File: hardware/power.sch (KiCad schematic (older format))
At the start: 1 part, among them U5 MCP1755

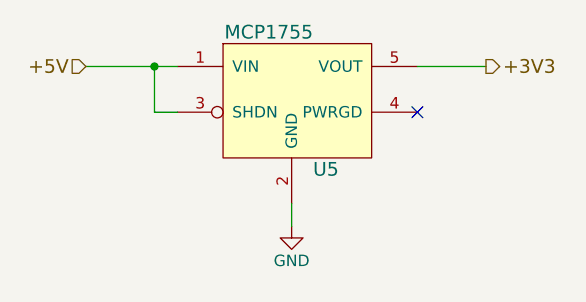
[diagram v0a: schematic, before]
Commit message: devboard fixed, added LED, Added Capacitor, Changed CAN chips
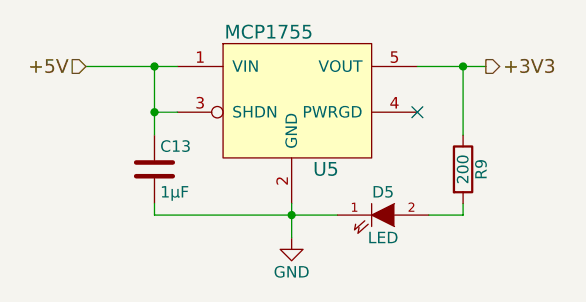
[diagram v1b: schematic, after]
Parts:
- added C13: 1μF, Capacitors_SMD:C_0603, symbol C
- added D5: LED, LEDs:LED_0805, symbol LED
- added R9: 200, Resistors_SMD:R_0603_HandSoldering, symbol R
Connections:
- net +3V3: now also R9.1
- net +5V: now also C13.1
- net GND: now also C13.2, D5.1 (K)
- new net: D5.2 (A), R9.2
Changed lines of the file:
@@
 	3900 2600 4300 2600
 Wire Wire Line
-	4200 2600 4200 2800
+	4200 2600 4200 2900
 Wire Wire Line
 	4200 2800 4300 2800
 Connection ~ 4200 2600
 $Comp
-L GND #PWR032
+L GND #PWR029
 U 1 1 55FDA4E7
-P 4800 3300
-F 0 "#PWR032" H 4800 3050 50  0001 C CNN
-F 1 "GND" H 4800 3150 50  0000 C CNN
-F 2 "" H 4800 3300 60  0000 C CNN
-F 3 "" H 4800 3300 60  0000 C CNN
-	1    4800 3300
+P 4800 3350
+F 0 "#PWR029" H 4800 3100 50  0001 C CNN
+F 1 "GND" H 4800 3200 50  0000 C CNN
+F 2 "" H 4800 3350 60  0000 C CNN
+F 3 "" H 4800 3350 60  0000 C CNN
+	1    4800 3350
 	1    0    0    -1
 $EndComp
 Wire Wire Line
-	4800 3200 4800 3300
+	4800 3200 4800 3350
 Wire Wire Line
 	5350 2600 5650 2600
@@
 Text HLabel 5650 2600 2    60   Output ~ 0
 +3V3
+$Comp
+L R R9
+U 1 1 568ED20B
+P 5550 3050
+F 0 "R9" V 5630 3050 50  0000 C CNN
+F 1 "200" V 5550 3050 50  0000 C CNN
+F 2 "Resistors_SMD:R_0603_HandSoldering" H 5480 3050 50  0001 C CNN
+F 3 "" H 5550 3050 50  0000 C CNN
+	1    5550 3050
+	1    0    0    -1
+$EndComp
+Wire Wire Line
+	5550 2600 5550 2900
+Connection ~ 5550 2600
+$Comp
+L LED D5
+U 1 1 568ED2B8
+P 5200 3250
+F 0 "D5" H 5200 3350 50  0000 C CNN
+F 1 "LED" H 5200 3150 50  0000 C CNN
+F 2 "LEDs:LED_0805" H 5200 3250 50  0001 C CNN
+F 3 "" H 5200 3250 50  0000 C CNN
+	1    5200 3250
+	1    0    0    -1
+$EndComp
+Wire Wire Line
+	4200 3250 5000 3250
+Connection ~ 4800 3250
+Wire Wire Line
+	5550 3200 5550 3250
+Wire Wire Line
+	5550 3250 5400 3250
+$Comp
+L C C13
+U 1 1 568EDCCD
+P 4200 3050
+F 0 "C13" H 4225 3150 50  0000 L CNN
+F 1 "1μF" H 4225 2950 50  0000 L CNN
+F 2 "Capacitors_SMD:C_0603" H 4238 2900 50  0001 C CNN
+F 3 "" H 4200 3050 50  0000 C CNN
+	1    4200 3050
+	1    0    0    -1
+$EndComp
+Connection ~ 4200 2800
+Wire Wire Line
+	4200 3200 4200 3250
 $EndSCHEMATC
